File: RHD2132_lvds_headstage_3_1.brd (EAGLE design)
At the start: 100 x 80 mm, 15 parts, among them U1 RHD2132_QFN

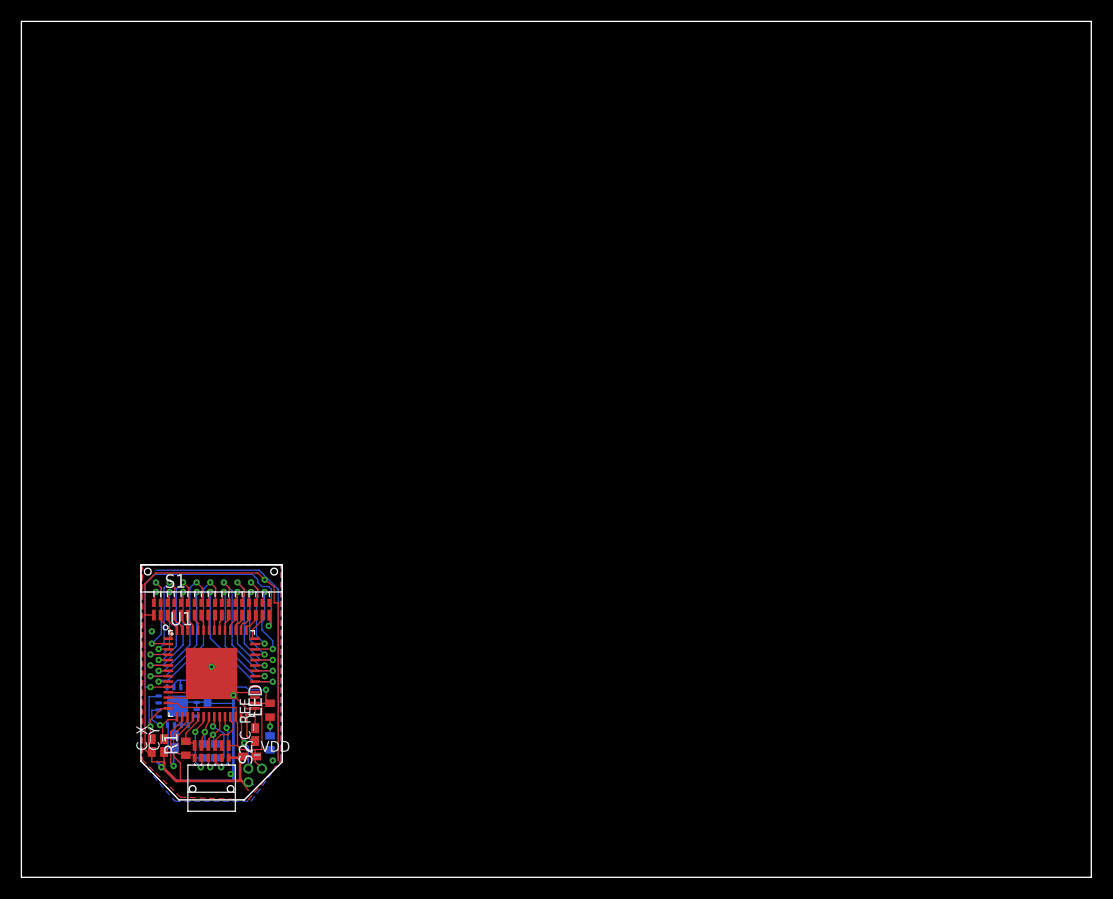
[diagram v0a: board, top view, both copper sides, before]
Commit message: Add Illustrator file for headstages
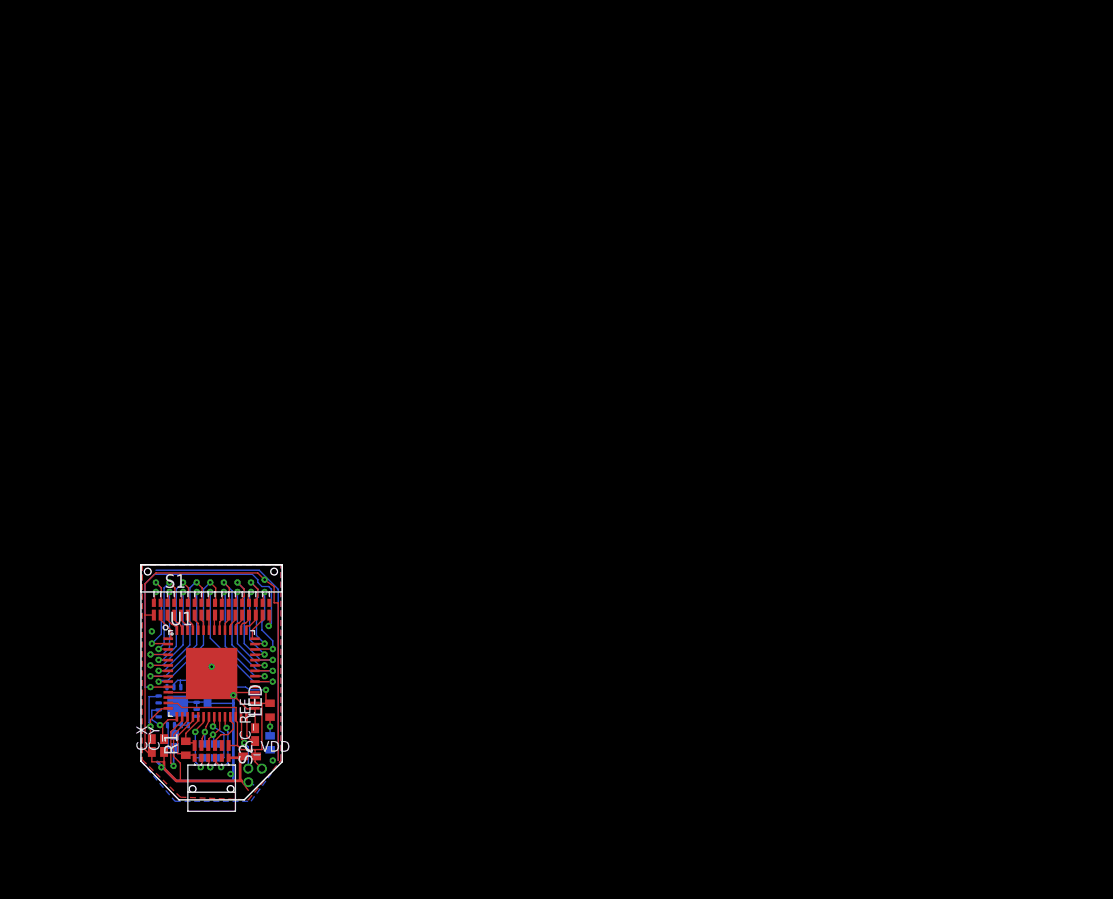
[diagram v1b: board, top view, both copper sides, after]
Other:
- board size 100 x 80 mm -> 13.2 x 22 mm
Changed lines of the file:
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@@
 <layer number="1" name="Top" color="4" fill="1" visible="yes" active="yes"/>
 <layer number="16" name="Bottom" color="9" fill="1" visible="yes" active="yes"/>
-<layer number="17" name="Pads" color="2" fill="1" visible="no" active="yes"/>
+<layer number="17" name="Pads" color="2" fill="1" visible="yes" active="yes"/>
 <layer number="18" name="Vias" color="2" fill="1" visible="yes" active="yes"/>
 <layer number="19" name="Unrouted" color="6" fill="1" visible="no" active="yes"/>
 <layer number="20" name="Dimension" color="15" fill="1" visible="yes" active="yes"/>
-<layer number="21" name="tPlace" color="7" fill="1" visible="yes" active="yes"/>
+<layer number="21" name="tPlace" color="7" fill="1" visible="no" active="yes"/>
 <layer number="22" name="bPlace" color="7" fill="1" visible="no" active="yes"/>
-<layer number="23" name="tOrigins" color="15" fill="1" visible="yes" active="yes"/>
+<layer number="23" name="tOrigins" color="15" fill="1" visible="no" active="yes"/>
 <layer number="24" name="bOrigins" color="15" fill="1" visible="no" active="yes"/>
 <layer number="25" name="tNames" color="7" fill="1" visible="no" active="yes"/>
@@
 <layer number="29" name="tStop" color="7" fill="3" visible="no" active="yes"/>
 <layer number="30" name="bStop" color="7" fill="6" visible="no" active="yes"/>
-<layer number="31" name="tCream" color="7" fill="4" visible="yes" active="yes"/>
+<layer number="31" name="tCream" color="7" fill="4" visible="no" active="yes"/>
 <layer number="32" name="bCream" color="7" fill="5" visible="no" active="yes"/>
 <layer number="33" name="tFinish" color="6" fill="3" visible="no" active="yes"/>
@@
 <layer number="42" name="bRestrict" color="1" fill="10" visible="no" active="yes"/>
 <layer number="43" name="vRestrict" color="2" fill="10" visible="no" active="yes"/>
-<layer number="44" name="Drills" color="7" fill="1" visible="yes" active="yes"/>
-<layer number="45" name="Holes" color="7" fill="1" visible="yes" active="yes"/>
-<layer number="46" name="Milling" color="3" fill="1" visible="yes" active="yes"/>
+<layer number="44" name="Drills" color="7" fill="1" visible="no" active="yes"/>
+<layer number="45" name="Holes" color="7" fill="1" visible="no" active="yes"/>
+<layer number="46" name="Milling" color="3" fill="1" visible="no" active="yes"/>
 <layer number="47" name="Measures" color="7" fill="1" visible="no" active="yes"/>
 <layer number="48" name="Document" color="7" fill="1" visible="no" active="yes"/>
 <layer number="49" name="Reference" color="7" fill="1" visible="no" active="yes"/>
 <layer number="50" name="dxf" color="7" fill="1" visible="no" active="no"/>
-<layer number="51" name="tDocu" color="15" fill="1" visible="yes" active="yes"/>
-<layer number="52" name="bDocu" color="15" fill="1" visible="no" active="yes"/>
+<layer number="51" name="tDocu" color="13" fill="1" visible="yes" active="yes"/>
+<layer number="52" name="bDocu" color="13" fill="1" visible="yes" active="yes"/>
 <layer number="91" name="Nets" color="2" fill="1" visible="no" active="no"/>
 <layer number="92" name="Busses" color="1" fill="1" visible="no" active="no"/>
@@
 <board>
 <plain>
-<wire x1="0" y1="0" x2="100" y2="0" width="0" layer="20"/>
-<wire x1="100" y1="0" x2="100" y2="80" width="0" layer="20"/>
-<wire x1="100" y1="80" x2="0" y2="80" width="0" layer="20"/>
-<wire x1="0" y1="80" x2="0" y2="0" width="0" layer="20"/>
 <hole x="11.811" y="28.575" drill="0.635"/>
 <hole x="23.622" y="28.575" drill="0.635"/>

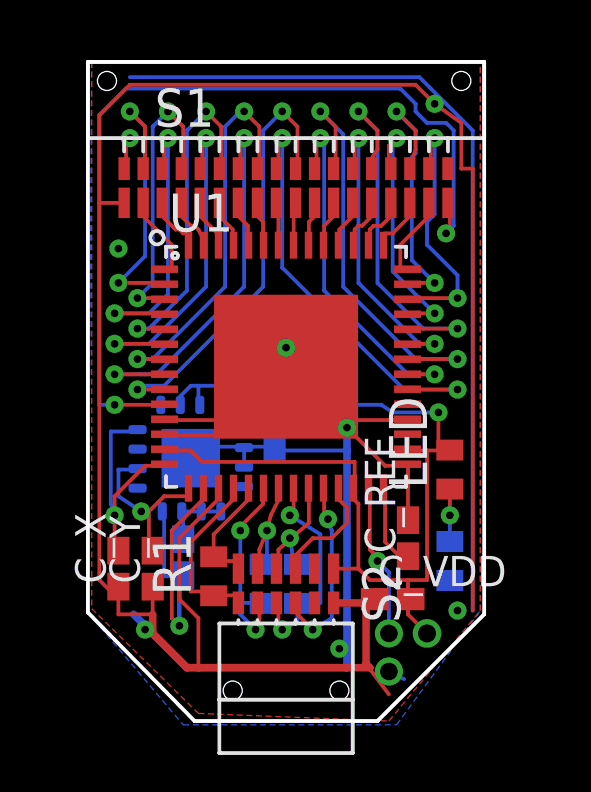
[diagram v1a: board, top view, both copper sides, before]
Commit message: flipped gnd and ref to make the pinout plexon etc. compatible
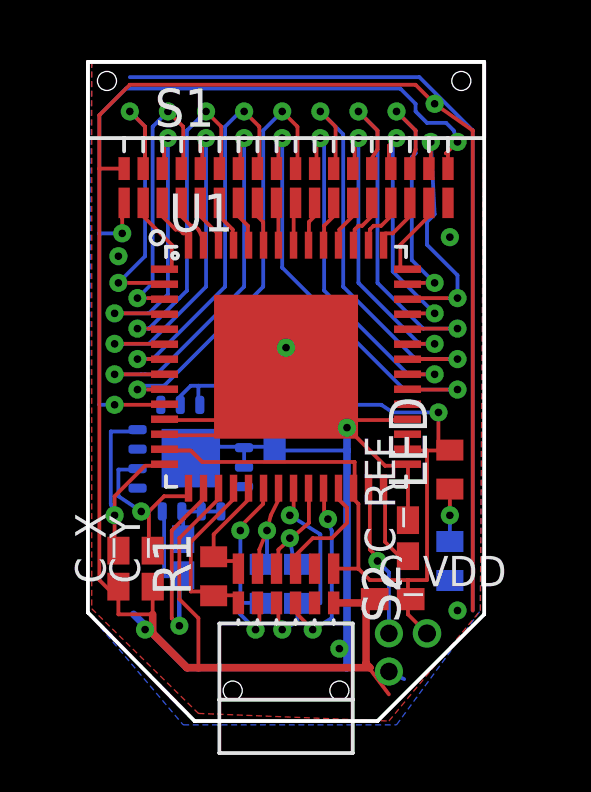
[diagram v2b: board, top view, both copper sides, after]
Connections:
- net GND: now also S1.B1, S1.T18; no longer S1.B18, S1.T1
- net REF: now also S1.B18, S1.T1; no longer S1.B1, S1.T18
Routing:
- net REF: track 31.3 -> 28.0 mm
- net GND: track 135.9 -> 135.7 mm, vias 8 -> 9
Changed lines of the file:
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@@
 <layers>
 <layer number="1" name="Top" color="4" fill="1" visible="yes" active="yes"/>
-<layer number="16" name="Bottom" color="9" fill="1" visible="yes" active="yes"/>
+<layer number="16" name="Bottom" color="9" fill="1" visible="no" active="yes"/>
 <layer number="17" name="Pads" color="2" fill="1" visible="yes" active="yes"/>
 <layer number="18" name="Vias" color="2" fill="1" visible="yes" active="yes"/>
-<layer number="19" name="Unrouted" color="6" fill="1" visible="no" active="yes"/>
+<layer number="19" name="Unrouted" color="6" fill="1" visible="yes" active="yes"/>
 <layer number="20" name="Dimension" color="15" fill="1" visible="yes" active="yes"/>
 <layer number="21" name="tPlace" color="7" fill="1" visible="no" active="yes"/>
@@
 <hole x="19.558" y="8.255" drill="0.635"/>
 <text x="22.225" y="12.954" size="0.8128" layer="51" font="vector" ratio="16" rot="R270">vcc</text>
+<rectangle x1="11.43" y1="15.748" x2="13.208" y2="17.399" layer="51"/>
+<rectangle x1="12.827" y1="8.001" x2="14.605" y2="9.652" layer="51"/>
 </plain>
 <attributes>
@@
 <signals>
 <signal name="REF">
-<contactref element="S1" pad="B1"/>
-<contactref element="S1" pad="T18"/>
 <contactref element="U1" pad="10"/>
-<via x="12.573" y="26.67" extent="1-16" drill="0.254"/>
-<wire x1="12.446" y1="25.908" x2="12.446" y2="26.543" width="0.127" layer="1"/>
-<wire x1="12.446" y1="26.543" x2="12.573" y2="26.67" width="0.127" layer="1"/>
-<wire x1="12.573" y1="26.67" x2="11.557" y2="26.67" width="0.127" layer="16"/>
-<wire x1="11.557" y1="26.67" x2="11.557" y2="17.78" width="0.127" layer="16"/>
+<via x="12.319" y="23.495" extent="1-16" drill="0.254"/>
+<wire x1="12.446" y1="24.511" x2="12.319" y2="24.003" width="0.127" layer="1"/>
+<wire x1="12.319" y1="24.003" x2="12.319" y2="23.495" width="0.127" layer="1"/>
+<wire x1="12.319" y1="23.495" x2="11.557" y2="23.495" width="0.127" layer="16"/>
+<wire x1="11.557" y1="23.495" x2="11.557" y2="17.78" width="0.127" layer="16"/>
 <wire x1="11.557" y1="17.78" x2="12.065" y2="17.78" width="0.127" layer="16"/>
 <via x="12.065" y="17.78" extent="1-16" drill="0.254"/>
-<wire x1="11.557" y1="26.67" x2="11.557" y2="27.432" width="0.127" layer="16"/>
+<wire x1="11.557" y1="23.495" x2="11.557" y2="27.432" width="0.127" layer="16"/>
 <wire x1="11.557" y1="27.432" x2="12.446" y2="28.321" width="0.127" layer="16"/>
 <wire x1="12.446" y1="28.321" x2="21.59" y2="28.321" width="0.127" layer="16"/>
-<via x="23.114" y="23.495" extent="1-16" drill="0.254"/>
+<via x="23.495" y="26.543" extent="1-16" drill="0.254"/>
 <wire x1="21.59" y1="28.321" x2="22.098" y2="27.813" width="0.127" layer="16"/>
 <wire x1="22.098" y1="27.813" x2="22.098" y2="27.559" width="0.127" layer="16"/>
@@
 <wire x1="22.479" y1="27.178" x2="23.114" y2="27.178" width="0.127" layer="16"/>
 <wire x1="23.114" y1="27.178" x2="23.368" y2="26.924" width="0.127" layer="16"/>
-<wire x1="23.368" y1="26.924" x2="23.368" y2="23.749" width="0.127" layer="16"/>
-<wire x1="23.368" y1="23.749" x2="23.114" y2="23.495" width="0.127" layer="16"/>
-<wire x1="23.241" y1="24.638" x2="23.241" y2="23.622" width="0.127" layer="1"/>
-<wire x1="23.241" y1="23.622" x2="23.114" y2="23.495" width="0.127" layer="1"/>
+<wire x1="23.368" y1="26.924" x2="23.495" y2="26.543" width="0.127" layer="16"/>
+<wire x1="23.114" y1="26.162" x2="23.495" y2="26.543" width="0.127" layer="1"/>
 <wire x1="13.716" y1="17.78" x2="12.065" y2="17.78" width="0.127" layer="1"/>
-<wire x1="23.241" y1="24.638" x2="23.1775" y2="24.511" width="0" layer="19" extent="1-1"/>
+<contactref element="S1" pad="B18"/>
+<wire x1="23.114" y1="26.162" x2="23.1775" y2="26.162" width="0.127" layer="1"/>
+<wire x1="23.1775" y1="26.162" x2="23.1775" y2="25.654" width="0.127" layer="1"/>
+<contactref element="S1" pad="T1"/>
+<wire x1="12.446" y1="24.511" x2="12.3825" y2="24.511" width="0" layer="19" extent="1-1"/>
 <wire x1="13.73" y1="17.8" x2="13.716" y2="17.78" width="0" layer="19" extent="1-1"/>
-<wire x1="12.3825" y1="25.654" x2="12.446" y2="25.908" width="0" layer="19" extent="1-1"/>
 </signal>
 <signal name="CS-">
@@
 <wire x1="15.494" y1="14.224" x2="14.986" y2="14.224" width="0.127" layer="16"/>
 <contactref element="S2" pad="B6"/>
-<contactref element="S1" pad="B18"/>
-<contactref element="S1" pad="T1"/>
 <contactref element="C_VDD" pad="1"/>
 <contactref element="C_A" pad="2"/>
@@
 <wire x1="14.859" y1="10.668" x2="14.859" y2="9.017" width="0.127" layer="1"/>
 <via x="19.558" y="9.652" extent="1-16" drill="0.254"/>
-<wire x1="11.557" y1="27.432" x2="11.557" y2="24.511" width="0.127" layer="1"/>
-<wire x1="11.557" y1="24.511" x2="11.557" y2="11.938" width="0.127" layer="1"/>
+<wire x1="11.557" y1="27.432" x2="11.557" y2="25.654" width="0.127" layer="1"/>
+<wire x1="11.557" y1="25.654" x2="11.557" y2="11.938" width="0.127" layer="1"/>
 <wire x1="11.557" y1="11.938" x2="12.192" y2="11.303" width="0.127" layer="1"/>
 <wire x1="12.192" y1="11.303" x2="12.192" y2="10.795" width="0.127" layer="1"/>
@@
 <wire x1="11.557" y1="27.432" x2="12.573" y2="28.448" width="0.127" layer="1"/>
 <wire x1="12.573" y1="28.448" x2="22.098" y2="28.448" width="0.127" layer="1"/>
-<wire x1="24.003" y1="25.654" x2="24.003" y2="10.922" width="0.127" layer="1"/>
-<wire x1="12.319" y1="24.511" x2="11.557" y2="24.511" width="0.127" layer="1"/>
-<wire x1="23.622" y1="25.654" x2="23.622" y2="27.178" width="0.127" layer="1"/>
-<wire x1="23.622" y1="27.178" x2="22.733" y2="27.813" width="0.127" layer="1"/>
+<wire x1="24.003" y1="26.924" x2="24.003" y2="10.922" width="0.127" layer="1"/>
+<wire x1="12.319" y1="25.654" x2="11.557" y2="25.654" width="0.127" layer="1"/>
+<wire x1="24.003" y1="26.924" x2="22.733" y2="27.813" width="0.127" layer="1"/>
 <wire x1="22.733" y1="27.813" x2="22.098" y2="28.448" width="0.127" layer="1"/>
-<wire x1="23.622" y1="25.654" x2="24.003" y2="25.654" width="0.127" layer="1"/>
 <polygon width="0.1524" layer="1" isolate="0.254">
 <vertex x="11.303" y="29.21"/>
@@
 <vertex x="21.209" y="7.239"/>
 <vertex x="24.257" y="10.922"/>
-<vertex x="24.257" y="29.21"/>
+<vertex x="24.384" y="29.21"/>
 </polygon>
 <polygon width="0.1524" layer="16" isolate="0.254">
@@
 <vertex x="21.463" y="7.112"/>
 <vertex x="24.257" y="10.922"/>
-<vertex x="24.257" y="29.21"/>
+<vertex x="24.384" y="29.21"/>
 </polygon>
 <via x="17.78" y="19.685" extent="1-16" drill="0.254"/>
@@
 <wire x1="24.003" y1="10.922" x2="24.003" y2="26.924" width="0.127" layer="16"/>
 <wire x1="21.717" y1="8.636" x2="21.209" y2="8.89" width="0.127" layer="16"/>
-<via x="12.192" y="22.987" extent="1-16" drill="0.254"/>
+<via x="12.192" y="22.733" extent="1-16" drill="0.254"/>
 <via x="22.733" y="27.813" extent="1-16" drill="0.254"/>
 <contactref element="U$1" pad="COM1"/>
@@
 <via x="23.495" y="10.922" extent="1-16" drill="0.254"/>
 <via x="13.081" y="10.287" extent="1-16" drill="0.254"/>
+<contactref element="S1" pad="B1"/>
+<contactref element="S1" pad="T18"/>
+<via x="23.241" y="23.368" extent="1-16" drill="0.254"/>
 <wire x1="21.83" y1="17.3" x2="21.844" y2="17.272" width="0" layer="19" extent="1-1"/>
 <wire x1="19.812" y1="17.018" x2="19.685" y2="17.145" width="0" layer="19" extent="1-1"/>
@@
 <wire x1="16.38" y1="16.352" x2="15.748" y2="16.764" width="0" layer="19" extent="1-16"/>
 <wire x1="16.38" y1="15.702" x2="16.38" y2="16.352" width="0" layer="19" extent="16-16"/>
+<wire x1="23.1775" y1="24.511" x2="24.003" y2="26.924" width="0" layer="19" extent="1-1"/>
 </signal>
 <signal name="IN15">
@@
 </signal>
 <signal name="IN25">
-<via x="22.733" y="26.67" extent="1-16" drill="0.254"/>
+<via x="22.606" y="26.543" extent="1-16" drill="0.254"/>
 <wire x1="22.606" y1="25.908" x2="22.606" y2="26.543" width="0.127" layer="1"/>
-<wire x1="22.606" y1="26.543" x2="22.733" y2="26.67" width="0.127" layer="1"/>
-<wire x1="22.733" y1="26.67" x2="22.733" y2="24.13" width="0.127" layer="16"/>
+<wire x1="22.606" y1="26.543" x2="22.733" y2="24.13" width="0.127" layer="16"/>
 <wire x1="22.733" y1="24.13" x2="22.479" y2="23.876" width="0.127" layer="16"/>
 <wire x1="22.479" y1="23.876" x2="22.479" y2="23.114" width="0.127" layer="16"/>
